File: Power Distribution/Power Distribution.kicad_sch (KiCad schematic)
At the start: 11 parts, among them P1 ChargingBoardTP4056, SW1 Switch, U1 Raspberry Pi Zero 2 W, U5 IMU BNO55

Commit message: fix charging board
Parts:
- added ArducamToFCamera1: ~, symbol Camera:ArducamToFCam
- P1: value ChargingBoardTP4056 -> Charging/BoostConverterBoardTP4056&MT3608
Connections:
- net at C1.1, DAC.2 (GND), P1.A2 (Vout-)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: now also ArducamToFCamera1.2 (GND)
- net at C1.2, PiOLED.2 (+5V), PiOLED.4 (+5V)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: now also ArducamToFCamera1.1 (5V)
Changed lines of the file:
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@@
+		)
+	)
+	(text "5V"
+		(exclude_from_sim no)
+		(at 221.234 23.114 0)
+		(effects
+			(font
+				(size 1.27 1.27)
+			)
 		)
 	)
@@
 	)
 	(junction
+		(at 227.33 90.17)
+		(diameter 0)
+		(color 0 0 0 0)
+	)
+	(junction
 		(at 138.43 64.77)
+		(diameter 0)
+		(color 0 0 0 0)
+	)
+	(junction
+		(at 138.43 54.61)
 		(diameter 0)
 		(color 0 0 0 0)
@@
 	(wire
 		(pts
+			(xy 223.52 118.11) (xy 223.52 80.01)
+		)
+		(stroke
+			(width 0)
+			(type default)
+		)
+	)
+	(wire
+		(pts
 			(xy 149.86 85.09) (xy 143.51 85.09)
 		)
@@
 	(wire
 		(pts
+			(xy 138.43 54.61) (xy 140.97 54.61)
+		)
+		(stroke
+			(width 0)
+			(type default)
+		)
+	)
+	(wire
+		(pts
 			(xy 215.9 34.29) (xy 222.25 34.29)
 		)
@@
 	(wire
 		(pts
+			(xy 140.97 118.11) (xy 223.52 118.11)
+		)
+		(stroke
+			(width 0)
+			(type default)
+		)
+	)
+	(wire
+		(pts
 			(xy 210.82 41.91) (xy 218.44 41.91)
 		)
@@
 	(wire
 		(pts
+			(xy 138.43 54.61) (xy 138.43 57.15)
+		)
+		(stroke
+			(width 0)
+			(type default)
+		)
+	)
+	(wire
+		(pts
 			(xy 142.24 35.56) (xy 142.24 27.94)
 		)
@@
 	(wire
 		(pts
+			(xy 140.97 54.61) (xy 140.97 118.11)
+		)
+		(stroke
+			(width 0)
+			(type default)
+		)
+	)
+	(wire
+		(pts
 			(xy 261.62 49.53) (xy 261.62 57.15)
 		)
@@
 	(wire
 		(pts
+			(xy 227.33 82.55) (xy 227.33 90.17)
+		)
+		(stroke
+			(width 0)
+			(type default)
+		)
+	)
+	(wire
+		(pts
 			(xy 104.14 64.77) (xy 138.43 64.77)
 		)
@@
 	(wire
 		(pts
-			(xy 138.43 35.56) (xy 138.43 57.15)
-		)
-		(stroke
-			(width 0)
-			(type default)
-		)
-	)
-	(wire
-		(pts
-			(xy 217.17 90.17) (xy 252.73 90.17)
+			(xy 138.43 35.56) (xy 138.43 54.61)
+		)
+		(stroke
+			(width 0)
+			(type default)
+		)
+	)
+	(wire
+		(pts
+			(xy 223.52 80.01) (xy 227.33 80.01)
+		)
+		(stroke
+			(width 0)
+			(type default)
+		)
+	)
+	(wire
+		(pts
+			(xy 217.17 90.17) (xy 227.33 90.17)
 		)
 		(stroke
@@
 		(pts
 			(xy 114.3 40.64) (xy 111.76 40.64)
+		)
+		(stroke
+			(width 0)
+			(type default)
+		)
+	)
+	(wire
+		(pts
+			(xy 227.33 90.17) (xy 252.73 90.17)
 		)
 		(stroke
@@
 		(on_board yes)
 		(dnp no)
-		(fields_autoplaced yes)
 		(property "Reference" "P1"
 			(at 88.9 44.45 0)
@@
 			)
 		)
-		(property "Value" "ChargingBoardTP4056"
-			(at 88.9 49.53 0)
+		(property "Value" "Charging/BoostConverterBoardTP4056&MT3608"
+			(at 76.454 73.914 90)
 			(effects
 				(font
@@
 					(unit 1)
 				)
+			)
+		)
+	)
+	(symbol
+		(lib_id "Camera:ArducamToFCam")
+		(at 234.95 77.47 0)
+		(unit 1)
+		(exclude_from_sim no)
+		(in_bom yes)
+		(on_board yes)
+		(dnp no)
+		(fields_autoplaced yes)
+		(property "Reference" "ArducamToFCamera1"
+			(at 240.03 80.6449 0)
+			(effects
+				(font
+					(size 1.27 1.27)
+				)
+				(justify left)
+			)
+		)
+		(property "Value" "~"
+			(at 240.03 82.55 0)
+			(effects
+				(font
+					(size 1.27 1.27)
+				)
+				(justify left)
+			)
+		)
+		(property "Footprint" ""
+			(at 234.95 77.47 0)
+			(effects
+				(font
+					(size 1.27 1.27)
+				)
+				(hide yes)
+			)
+		)
+		(property "Datasheet" ""
+			(at 234.95 77.47 0)
+			(effects
+				(font
+					(size 1.27 1.27)
+				)
+				(hide yes)
+			)
+		)
+		(property "Description" ""
+			(at 234.95 77.47 0)
+			(effects
+				(font
+					(size 1.27 1.27)
+				)
+				(hide yes)
+			)
+		)
+		(pin "2"
+		)
+		(pin "1"
+		)
+		(instances
+			(project ""
+				(path "/ec1b8d42-e234-41e0-8bcf-2b2f52e7d9b3"
+					(reference "ArducamToFCamera1")
+					(unit 1)
+				)

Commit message: PCB update
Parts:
- removed C1: 47uF, 47uF:CAPC3225X280N, symbol GCJ32ER70J476KE01L:GCJ32ER70J476KE01L
- removed R1: 47kΩ, 47k:RES_ERA6ARW473V, symbol ERA6ARW473V:ERA6ARW473V
- added 1: ~, Adafruit LC709203F LiPoly LiIon Fuel Gauge and Battery Monitor:WDFN8_3X4_0.65, symbol LC709203F:LC709203F
- added R1: Thermistor 10k, RES_NCU15X_MUR, symbol Thermistor 10k:NCU15XH103F6SRC
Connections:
- net at ArducamToFCamera1.2 (GND), DAC.2 (GND), P1.A2 (Vout-)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: now also 1.2 (VSS), R1.1
- net at SW1.2 (B): now also ArducamToFCamera1.1 (5V), PiOLED.2 (+5V), PiOLED.4 (+5V), U1.2 (5V_2), 1.3 (VDD)
- net at U1.22 (GPIO25/GPIO_GEN6): now also 1.7 (SDA)
- net at U1.23 (GPIO11/SPI_SCLK): now also 1.8 (SCL)
- new net: 1.4 (THERM), R1.2
- no-connect marks 40 -> 39

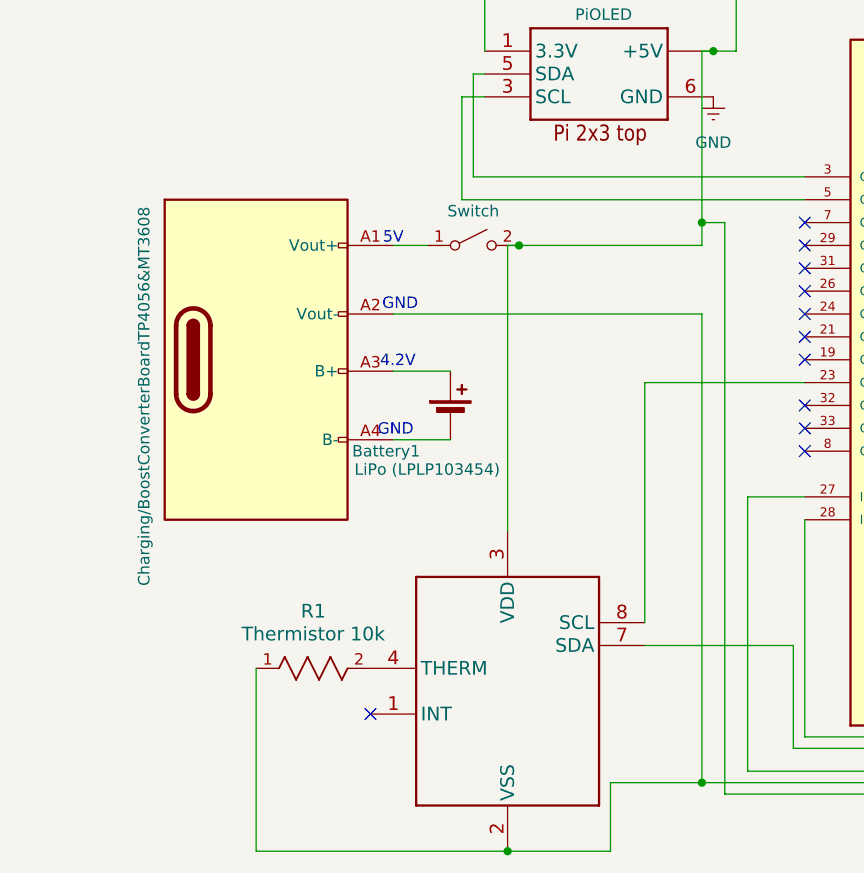
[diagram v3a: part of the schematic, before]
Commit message: Oled logo
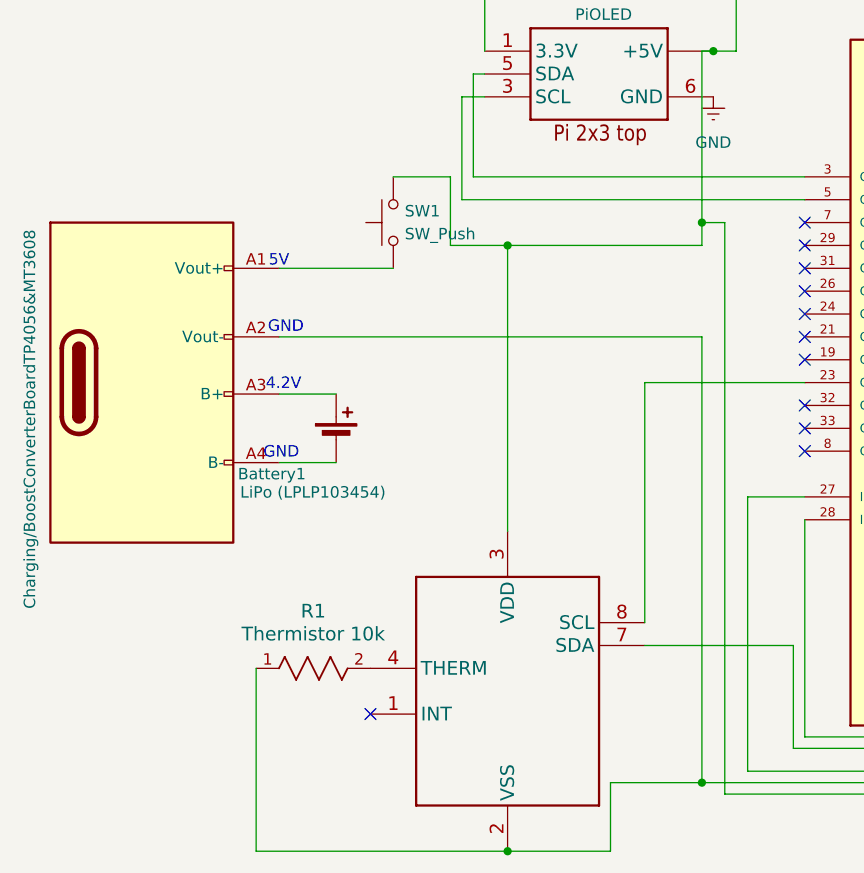
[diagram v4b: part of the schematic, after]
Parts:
- removed SW1: Switch, symbol Switch:SW_DPST_x2
- added SW1: SW_Push, symbol Switch:SW_Push
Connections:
- net at 1.3 (VDD), ArducamToFCamera1.1 (5V), PiOLED.2 (+5V)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: now also SW1.2
- net at P1.A1 (Vout+), P1.A9 (VBUS), P1.B4 (VBUS)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: now also SW1.1
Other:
- moved on the sheet: Battery1

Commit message: updated schematic and PCB
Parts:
- removed SW1: SW_Push, symbol Switch:SW_Push
- removed U5: IMU BNO55, 2472:MODULE_2472, symbol 2472:2472
- added IMU1: BNO055, IMU:MODULE_2472, symbol 2472:2472
- added SW1: Switch, symbol Switch:SW_DPST_x2
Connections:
- net GND: now also 1.2 (VSS), ArducamToFCamera1.2 (GND), DAC.2 (GND), P1.A2 (Vout-), R1.1, U1.6 (GND_6), IMU1.3 (GND)
- net at 1.7 (SDA): no longer U1.22 (GPIO25/GPIO_GEN6)
- net at 1.8 (SCL): no longer U1.23 (GPIO11/SPI_SCLK)
- net at P1.A1 (Vout+), P1.A9 (VBUS), P1.B4 (VBUS)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: now also SW1.1 (A)
- net at PiOLED.3 (SCL): no longer U1.5 (GPIO3/SCL)
- net at PiOLED.5 (SDA): no longer U1.3 (GPIO2/SDA1)
- net at U1.12 (GPIO18/GPIO_GEN1): no longer DAC.5 (BCK)
- net at U1.35 (GPIO19): no longer DAC.3 (LRCK)
- net at U1.4 (5V_4): no longer DAC.1 (VIN)
- net at U1.40 (GPIO21): no longer DAC.4 (DIN)
- new net: PiOLED.2 (+5V), PiOLED.4 (+5V)
- now unconnected: 1.3 (VDD), ArducamToFCamera1.1 (5V), DAC.11 (A3V3), PiOLED.1 (3.3V), U1.1 (3V3_1), U1.2 (5V_2)
- no-connect marks 39 -> 40
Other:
- note added: "Battery Fuel Gauge (LC709203F)"
- note added: "DAC (PCM5102a) and two speakers"
- note added: "IMU"
- note added: "PiOled"
- note added: "Power Source (battery, charging board, and boost converter)"
- note added: "Raspberry Pi Zero 2w"
- moved on the sheet: ArducamToFCamera1, Battery1, DAC, LS1, LS2, PiOLED, R1

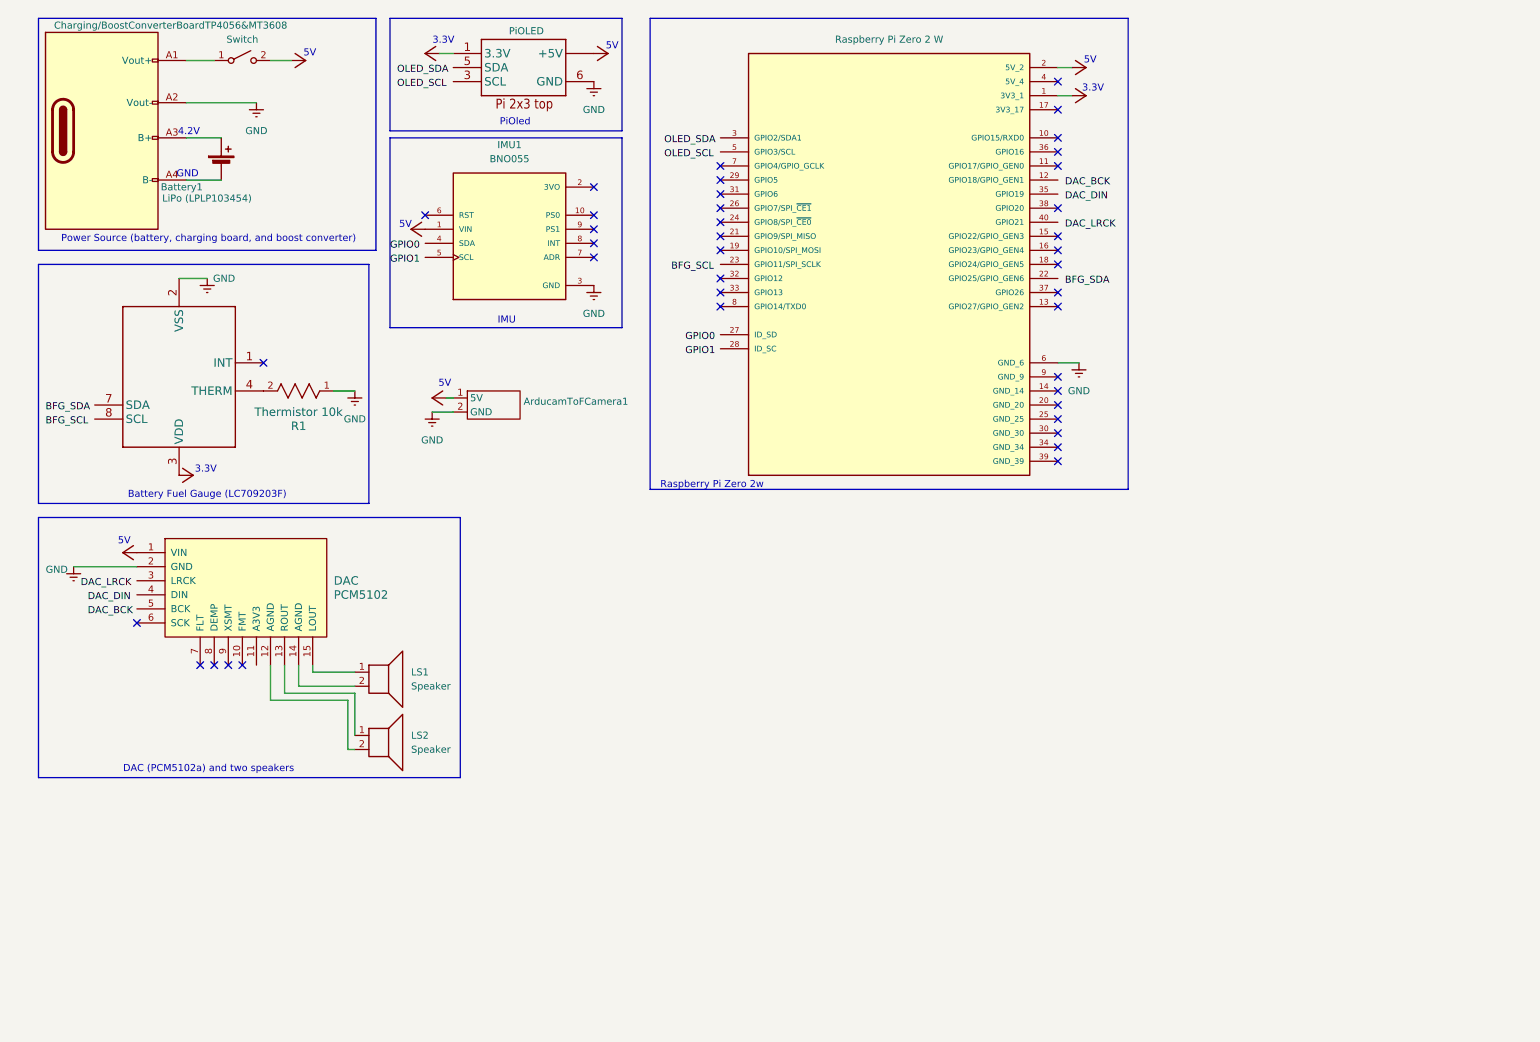
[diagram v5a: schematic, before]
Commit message: Updated schematic and PCB
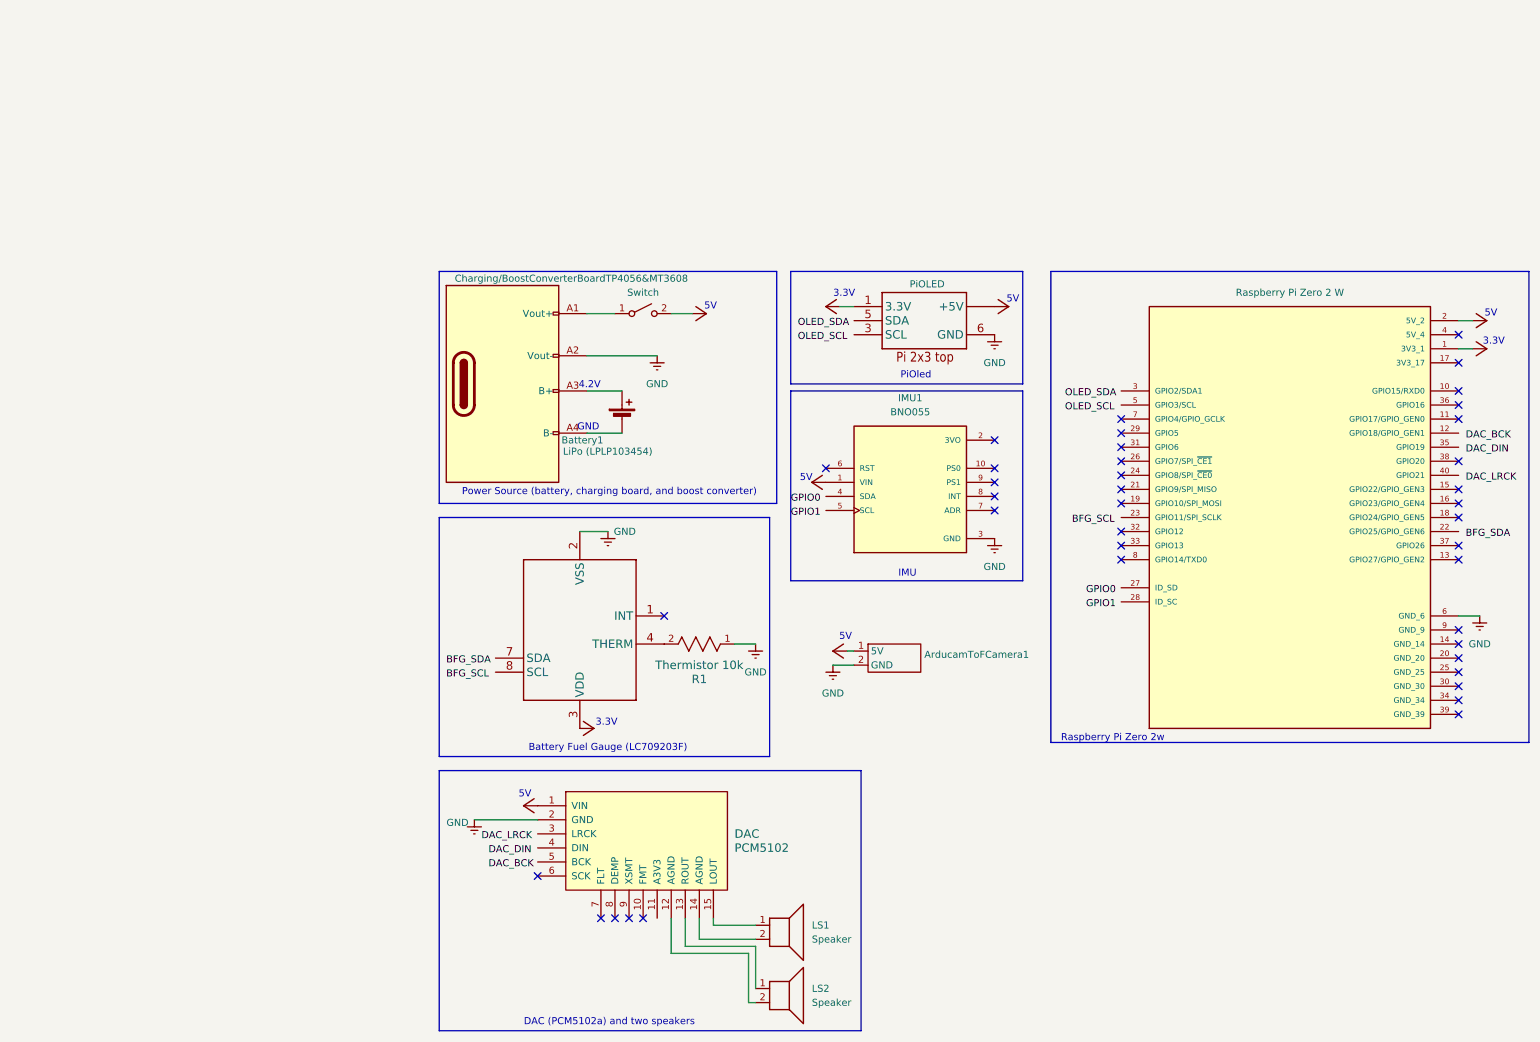
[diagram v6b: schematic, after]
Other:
- moved on the sheet: ArducamToFCamera1, Battery1, DAC, IMU1, LS1, LS2, PiOLED, R1

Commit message: PCB
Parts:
- removed SW1: Switch, symbol Switch:SW_DPST_x2
- added SW: SW_Push_LED, symbol Switch:SW_Push_LED
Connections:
- net GND: now also SW.3 (K)
- net at P1.A1 (Vout+), P1.A9 (VBUS), P1.B4 (VBUS)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: now also SW.2
- new net: SW.1, SW.4 (A)
- no-connect marks 40 -> 42
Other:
- moved on the sheet: ArducamToFCamera1, IMU1, PiOLED

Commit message: PCB
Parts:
- removed Battery1: LiPo (LPLP103454), symbol Device:Battery_Cell
- removed U1: Raspberry Pi Zero 2 W, Raspberry Pi Zero 2 w:MODULE_SC1176, symbol SC1176:SC1176
- added Battery1: ~, symbol Li-Poly Battery:Li-Poly_Battery
- added C1: 10nF, symbol Device:C
- added RGBCamera1: ~, symbol RGB Camera:RGB_Camera
- added U2: Raspberryt Pi Zero 2W, Raspberry Pi Zero 2 w:MODULE_SC1176, symbol SC1176:SC1176
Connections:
- net GND: now also C1.1, U2.6 (GND_6)
- net at P1.A1 (Vout+), P1.A9 (VBUS), P1.B4 (VBUS)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: now also C1.2
- net at P1.A3 (B+): now also Battery1.1 (+)
- net at P1.A4 (B-): now also Battery1.2 (-)
- net at DAC.3 (LRCK): now also U2.40 (GPIO21)
- net at DAC.4 (DIN): now also U2.35 (GPIO19)
- net at DAC.5 (BCK): now also U2.12 (GPIO18/GPIO_GEN1)
- net at IMU1.4 (SDA): now also U2.27 (ID_SD)
- net at IMU1.5 (SCL): now also U2.28 (ID_SC)
- new net: RGBCamera1. (USB_A), U2. (USB_A)
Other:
- note added: "USB-C Port"
- moved on the sheet: ArducamToFCamera1, DAC, IMU1, LS1, LS2, PiOLED, R1
